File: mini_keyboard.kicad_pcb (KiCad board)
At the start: 2 copper layers, 46 parts, among them SW1 SW_DIP_x01, SW10 SW_DIP_x01, SW11 SW_DIP_x01, SW12 SW_DIP_x01, SW13 SW_DIP_x01, SW14 SW_DIP_x01, SW15 SW_DIP_x01, SW16 SW_DIP_x01, SW17 SW_DIP_x01, SW18 SW_DIP_x01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

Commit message: gjort så många kablar som jag kan
Nästa steg är att göra kablar som hoppar på undersidan
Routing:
- net Net-(U1-PadGND): track 0.00 -> 317.5 mm
- net Net-(U1-Pad5V): track 0.00 -> 310.1 mm
- net Net-(U1-PadA1): track 0.00 -> 294.5 mm
- net Net-(U1-PadA0): track 0.00 -> 290.8 mm
- net Net-(U1-Pad7): track 0.00 -> 224.0 mm
- net Net-(D10-Pad1): track 0.00 -> 122.6 mm
- net Net-(D14-Pad1): track 0.00 -> 102.5 mm
- net Net-(D13-Pad1): track 0.00 -> 82.4 mm
- net Net-(D12-Pad1): track 0.00 -> 62.3 mm
- net Net-(D1-Pad1): track 0.00 -> 42.2 mm
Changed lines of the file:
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@@
     (thickness 1.6)
     (drawings 0)
-    (tracks 47)
+    (tracks 100)
     (zones 0)
     (modules 46)
@@
   )
   (segment (start 102.87 53.34) (end 102.87 59.69) (width 0.25) (layer F.Cu) (net 1))
+  (segment (start 97.79 53.34) (end 97.79 49.53) (width 0.25) (layer F.Cu) (net 2))
+  (segment (start 97.79 49.53) (end 97.79 45.72) (width 0.25) (layer F.Cu) (net 2))
+  (segment (start 97.79 45.72) (end 97.79 41.91) (width 0.25) (layer F.Cu) (net 2))
+  (segment (start 80.986 41.91) (end 71.136 32.06) (width 0.25) (layer F.Cu) (net 2))
+  (segment (start 97.79 41.91) (end 80.986 41.91) (width 0.25) (layer F.Cu) (net 2))
   (segment (start 121.92 53.34) (end 121.92 59.69) (width 0.25) (layer F.Cu) (net 3))
+  (segment (start 116.84 53.34) (end 116.84 49.53) (width 0.25) (layer F.Cu) (net 4))
+  (segment (start 116.84 45.72) (end 116.84 41.91) (width 0.25) (layer F.Cu) (net 4))
+  (segment (start 116.84 49.53) (end 116.84 45.72) (width 0.25) (layer F.Cu) (net 4))
+  (segment (start 104.45 29.52) (end 71.136 29.52) (width 0.25) (layer F.Cu) (net 4))
+  (segment (start 116.84 41.91) (end 104.45 29.52) (width 0.25) (layer F.Cu) (net 4))
   (segment (start 140.97 53.34) (end 140.97 59.69) (width 0.25) (layer F.Cu) (net 5))
+  (segment (start 120.96 26.98) (end 71.136 26.98) (width 0.25) (layer F.Cu) (net 6))
+  (segment (start 135.89 41.91) (end 120.96 26.98) (width 0.25) (layer F.Cu) (net 6))
+  (segment (start 135.89 41.91) (end 135.89 45.72) (width 0.25) (layer F.Cu) (net 6))
+  (segment (start 135.89 45.72) (end 135.89 49.53) (width 0.25) (layer F.Cu) (net 6))
+  (segment (start 135.89 49.53) (end 135.89 53.34) (width 0.25) (layer F.Cu) (net 6))
   (segment (start 160.02 53.34) (end 160.02 59.69) (width 0.25) (layer F.Cu) (net 7))
+  (segment (start 137.47 24.44) (end 71.136 24.44) (width 0.25) (layer F.Cu) (net 8))
+  (segment (start 154.94 41.91) (end 137.47 24.44) (width 0.25) (layer F.Cu) (net 8))
+  (segment (start 154.94 53.34) (end 154.94 49.53) (width 0.25) (layer F.Cu) (net 8))
+  (segment (start 154.94 45.72) (end 154.94 41.91) (width 0.25) (layer F.Cu) (net 8))
+  (segment (start 154.94 49.53) (end 154.94 45.72) (width 0.25) (layer F.Cu) (net 8))
   (segment (start 179.07 53.34) (end 179.07 59.69) (width 0.25) (layer F.Cu) (net 9))
+  (segment (start 153.98 21.9) (end 71.136 21.9) (width 0.25) (layer F.Cu) (net 10))
+  (segment (start 173.99 41.91) (end 153.98 21.9) (width 0.25) (layer F.Cu) (net 10))
+  (segment (start 173.99 53.34) (end 173.99 49.53) (width 0.25) (layer F.Cu) (net 10))
+  (segment (start 173.99 49.53) (end 173.99 45.72) (width 0.25) (layer F.Cu) (net 10))
+  (segment (start 173.99 45.72) (end 173.99 41.91) (width 0.25) (layer F.Cu) (net 10))
   (segment (start 104.245001 77.364999) (end 102.87 78.74) (width 0.25) (layer F.Cu) (net 11))
   (segment (start 104.245001 50.905001) (end 104.245001 77.364999) (width 0.25) (layer F.Cu) (net 11))
@@
   (segment (start 182.41002 113.49998) (end 179.07 116.84) (width 0.25) (layer F.Cu) (net 25))
   (segment (start 179.07 41.91) (end 182.41002 45.25002) (width 0.25) (layer F.Cu) (net 25))
+  (segment (start 158.407002 19.36) (end 71.625001 19.36) (width 0.25) (layer F.Cu) (net 35))
+  (segment (start 193.04 53.992998) (end 158.407002 19.36) (width 0.25) (layer F.Cu) (net 35))
+  (segment (start 193.04 142.24) (end 193.04 53.992998) (width 0.25) (layer F.Cu) (net 35))
+  (segment (start 44.51997 28.31997) (end 55.88 39.68) (width 0.25) (layer F.Cu) (net 36))
+  (segment (start 44.51997 -5.577067) (end 44.51997 28.31997) (width 0.25) (layer F.Cu) (net 36))
+  (segment (start 45.222933 -6.28003) (end 44.51997 -5.577067) (width 0.25) (layer F.Cu) (net 36))
+  (segment (start 135.029768 -6.28003) (end 45.222933 -6.28003) (width 0.25) (layer F.Cu) (net 36))
+  (segment (start 203.2 61.890202) (end 135.029768 -6.28003) (width 0.25) (layer F.Cu) (net 36))
+  (segment (start 203.2 142.24) (end 203.2 61.890202) (width 0.25) (layer F.Cu) (net 36))
+  (segment (start 195.58 55.967299) (end 134.532701 -5.08) (width 0.25) (layer F.Cu) (net 45))
+  (segment (start 195.58 142.24) (end 195.58 55.967299) (width 0.25) (layer F.Cu) (net 45))
+  (segment (start 134.532701 -5.08) (end 45.72 -5.08) (width 0.25) (layer F.Cu) (net 45))
+  (segment (start 45.72 -5.08) (end 45.72 13.97) (width 0.25) (layer F.Cu) (net 45))
+  (segment (start 55.57 13.97) (end 55.88 14.28) (width 0.25) (layer F.Cu) (net 45))
+  (segment (start 45.72 13.97) (end 55.57 13.97) (width 0.25) (layer F.Cu) (net 45))
+  (segment (start 48.004301 16.82) (end 55.88 16.82) (width 0.25) (layer F.Cu) (net 46))
+  (segment (start 45.31999 -5.245689) (end 45.31999 14.135689) (width 0.25) (layer F.Cu) (net 46))
+  (segment (start 45.31999 14.135689) (end 48.004301 16.82) (width 0.25) (layer F.Cu) (net 46))
+  (segment (start 45.554311 -5.48001) (end 45.31999 -5.245689) (width 0.25) (layer F.Cu) (net 46))
+  (segment (start 198.12 57.9416) (end 134.69839 -5.48001) (width 0.25) (layer F.Cu) (net 46))
+  (segment (start 134.69839 -5.48001) (end 45.554311 -5.48001) (width 0.25) (layer F.Cu) (net 46))
+  (segment (start 198.12 142.24) (end 198.12 57.9416) (width 0.25) (layer F.Cu) (net 46))
+  (segment (start 44.91998 23.63998) (end 55.88 34.6) (width 0.25) (layer F.Cu) (net 48))
+  (segment (start 44.91998 -5.411378) (end 44.91998 23.63998) (width 0.25) (layer F.Cu) (net 48))
+  (segment (start 45.388622 -5.88002) (end 44.91998 -5.411378) (width 0.25) (layer F.Cu) (net 48))
+  (segment (start 134.864079 -5.88002) (end 45.388622 -5.88002) (width 0.25) (layer F.Cu) (net 48))
+  (segment (start 200.66 59.915901) (end 134.864079 -5.88002) (width 0.25) (layer F.Cu) (net 48))
+  (segment (start 200.66 142.24) (end 200.66 59.915901) (width 0.25) (layer F.Cu) (net 48))
 )

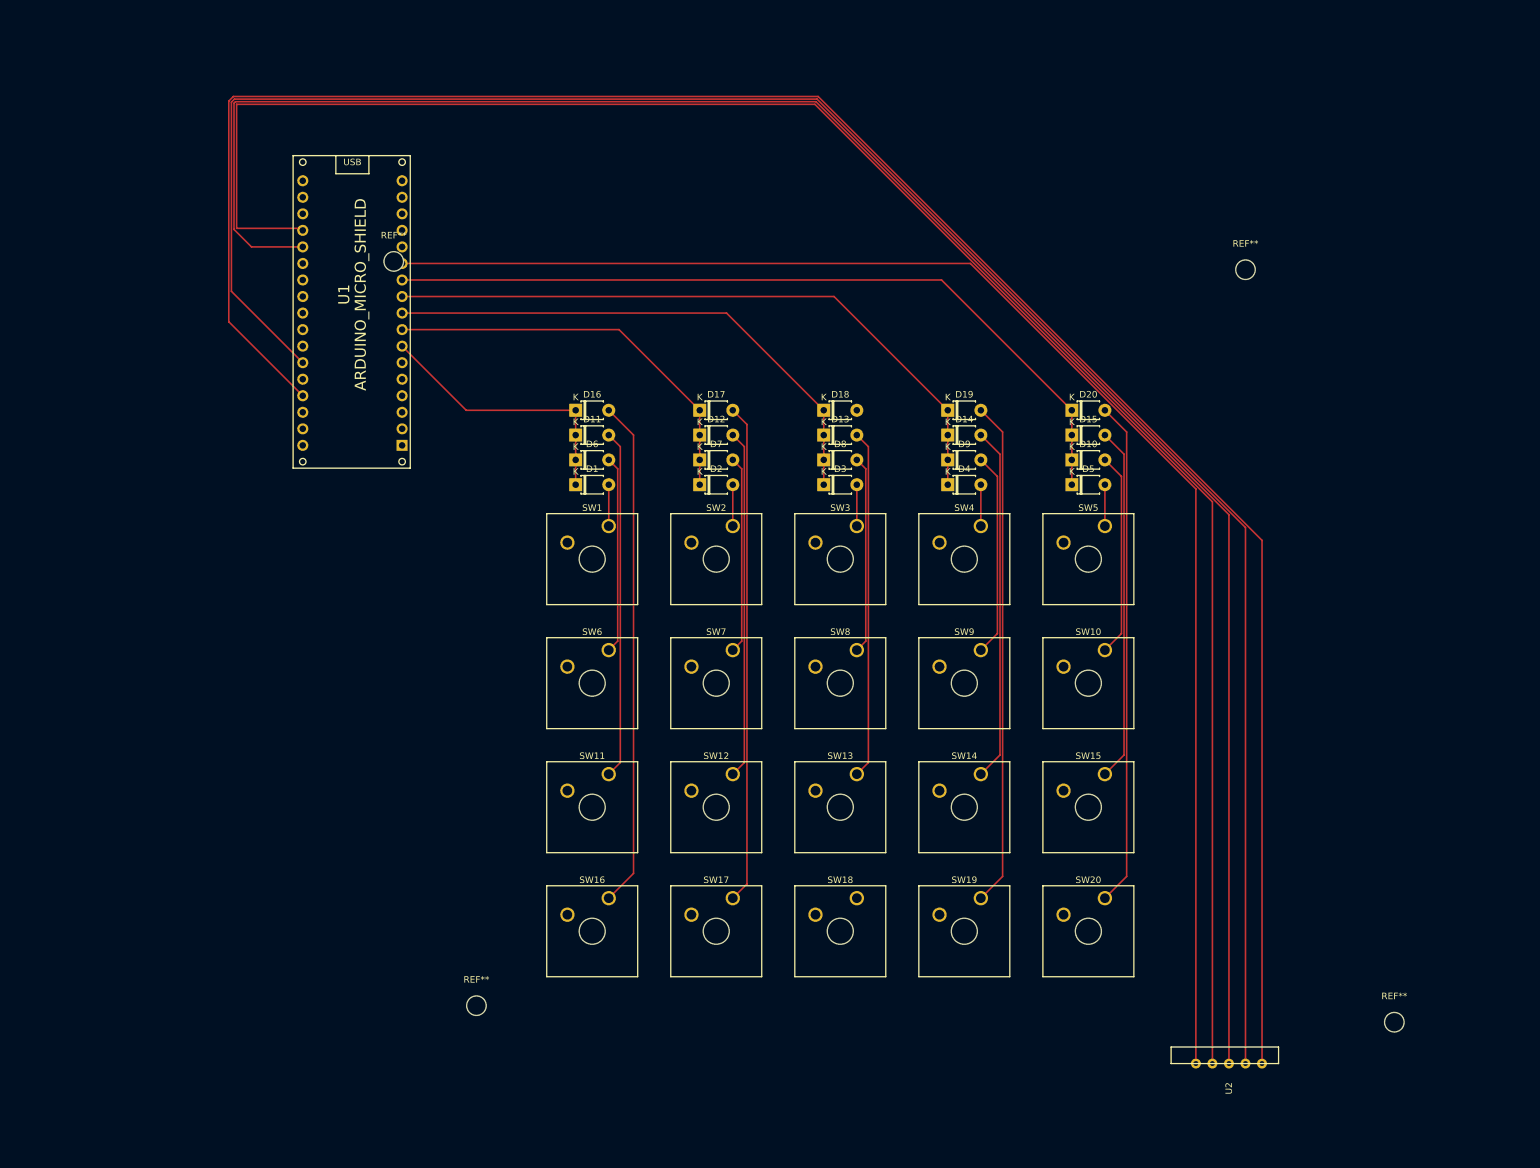
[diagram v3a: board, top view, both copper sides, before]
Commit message: made back and front cables
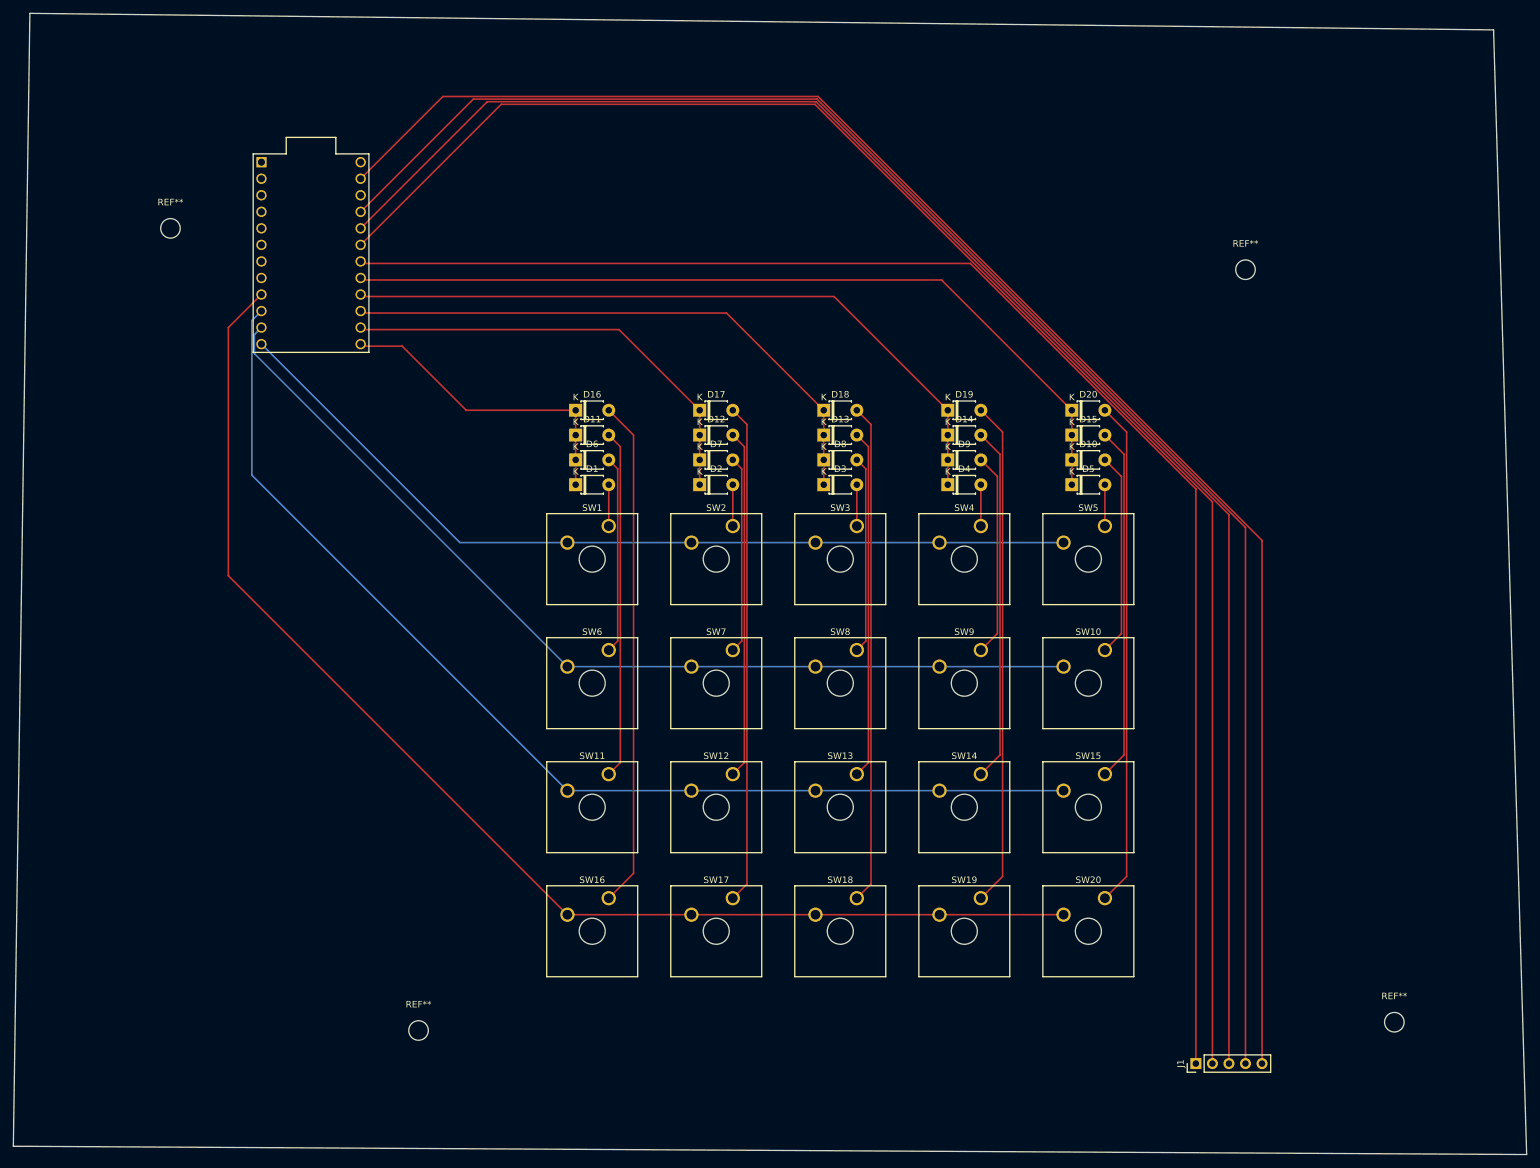
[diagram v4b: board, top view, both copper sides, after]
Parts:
- removed U2: Joystick, Joystick:Joystick
- added ?: , , F.Cu at (78.7, 133.3)
- added J1: Conn_01x05_Male, Connector_PinHeader_2.54mm:PinHeader_1x05_P2.54mm_Vertical, F.Cu at (193.0, 142.2)
- U1: value ARDUINO_MICRO_SHIELD -> ProMicro; footprint arduino_micro_shield:ARDUINO_MICRO_SHIELD -> promicro:ProMicro
- moved U1 36.4 mm to (57.1, 17.8), turned to 270 degrees
- moved REF** 34.7 mm to (35.6, 14.0)
- moved REF** 9.67 mm to (73.7, 137.2)
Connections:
- D1 pad 1: Net-(D1-Pad1) -> /in1
- D10 pad 1: Net-(D10-Pad1) -> /in5
- D11 pad 1: Net-(D1-Pad1) -> /in1
- D12 pad 1: Net-(D12-Pad1) -> /in2
- D13 pad 1: Net-(D13-Pad1) -> /in3
- D14 pad 1: Net-(D14-Pad1) -> /in4
- D15 pad 1: Net-(D10-Pad1) -> /in5
- D16 pad 1: Net-(D1-Pad1) -> /in1
- D17 pad 1: Net-(D12-Pad1) -> /in2
- D18 pad 1: Net-(D13-Pad1) -> /in3
- D19 pad 1: Net-(D14-Pad1) -> /in4
- D2 pad 1: Net-(D12-Pad1) -> /in2
- D20 pad 1: Net-(D10-Pad1) -> /in5
- D3 pad 1: Net-(D13-Pad1) -> /in3
- D4 pad 1: Net-(D14-Pad1) -> /in4
- D5 pad 1: Net-(D10-Pad1) -> /in5
- D6 pad 1: Net-(D1-Pad1) -> /in1
- D7 pad 1: Net-(D12-Pad1) -> /in2
- D8 pad 1: Net-(D13-Pad1) -> /in3
- D9 pad 1: Net-(D14-Pad1) -> /in4
- SW1 pad 2: Net-(SW1-Pad2) -> /out1
- SW10 pad 2: Net-(SW10-Pad2) -> /out2
- SW11 pad 2: Net-(SW11-Pad2) -> /out3
- SW12 pad 2: Net-(SW11-Pad2) -> /out3
- SW13 pad 2: Net-(SW11-Pad2) -> /out3
- SW14 pad 2: Net-(SW11-Pad2) -> /out3
- SW15 pad 2: Net-(SW11-Pad2) -> /out3
- SW16 pad 2: Net-(SW16-Pad2) -> /out4
- SW17 pad 2: Net-(SW16-Pad2) -> /out4
- SW18 pad 2: Net-(SW16-Pad2) -> /out4
- SW19 pad 2: Net-(SW16-Pad2) -> /out4
- SW2 pad 2: Net-(SW1-Pad2) -> /out1
- SW20 pad 2: Net-(SW16-Pad2) -> /out4
- SW3 pad 2: Net-(SW1-Pad2) -> /out1
- SW4 pad 2: Net-(SW1-Pad2) -> /out1
- SW5 pad 2: Net-(SW1-Pad2) -> /out1
- SW6 pad 2: Net-(SW10-Pad2) -> /out2
- SW7 pad 2: Net-(SW10-Pad2) -> /out2
- SW8 pad 2: Net-(SW10-Pad2) -> /out2
- SW9 pad 2: Net-(SW10-Pad2) -> /out2
- U1 pad 10: Net-(U1-Pad10) -> /out3
- U1 pad 11: Net-(U1-Pad11) -> /out2
- U1 pad 12: Net-(U1-Pad12) -> /out1
- U1 pad 13: Net-(U1-Pad13) -> /in1
- U1 pad 2: Net-(D1-Pad1) -> Net-(U1-Pad2)
- U1 pad 3: Net-(D12-Pad1) -> Net-(U1-Pad3)
- U1 pad 4: Net-(D13-Pad1) -> Net-(U1-Pad4)
- U1 pad 5: Net-(D14-Pad1) -> Net-(U1-Pad5)
- U1 pad 6: Net-(D10-Pad1) -> Net-(U1-Pad6)
- U1 pad 9: Net-(U1-Pad9) -> /out4
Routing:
- net Net-(U1-PadGND): track 317.5 -> 0.00 mm
- net Net-(U1-Pad5V): track 310.1 -> 0.00 mm
- net Net-(U1-PadA1): track 294.5 -> 0.00 mm
- net Net-(U1-PadA0): track 290.8 -> 0.00 mm
- net Net-(J1-Pad4): track 0.00 -> 252.6 mm
- net Net-(J1-Pad5): track 0.00 -> 252.2 mm
- net Net-(J1-Pad3): track 0.00 -> 252.0 mm
- net Net-(J1-Pad2): track 0.00 -> 251.3 mm
- net Net-(J1-Pad1): track 0.00 -> 231.0 mm
- net Net-(U1-Pad7): track 224.0 -> 0.00 mm
- net /out4: track 0.00 -> 195.1 mm
- net /out3: track 0.00 -> 170.5 mm
- net /out2: track 0.00 -> 148.6 mm
- net /out1: track 0.00 -> 135.8 mm
- net /in5: track 0.00 -> 129.1 mm
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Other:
- board outline added: 232.4 x 175.3 mm
